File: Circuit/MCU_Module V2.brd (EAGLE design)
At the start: 160 x 100 mm, 44 parts, among them IC1 75176BD, Q1 8MHZ, T1 BC848, T2 BC848

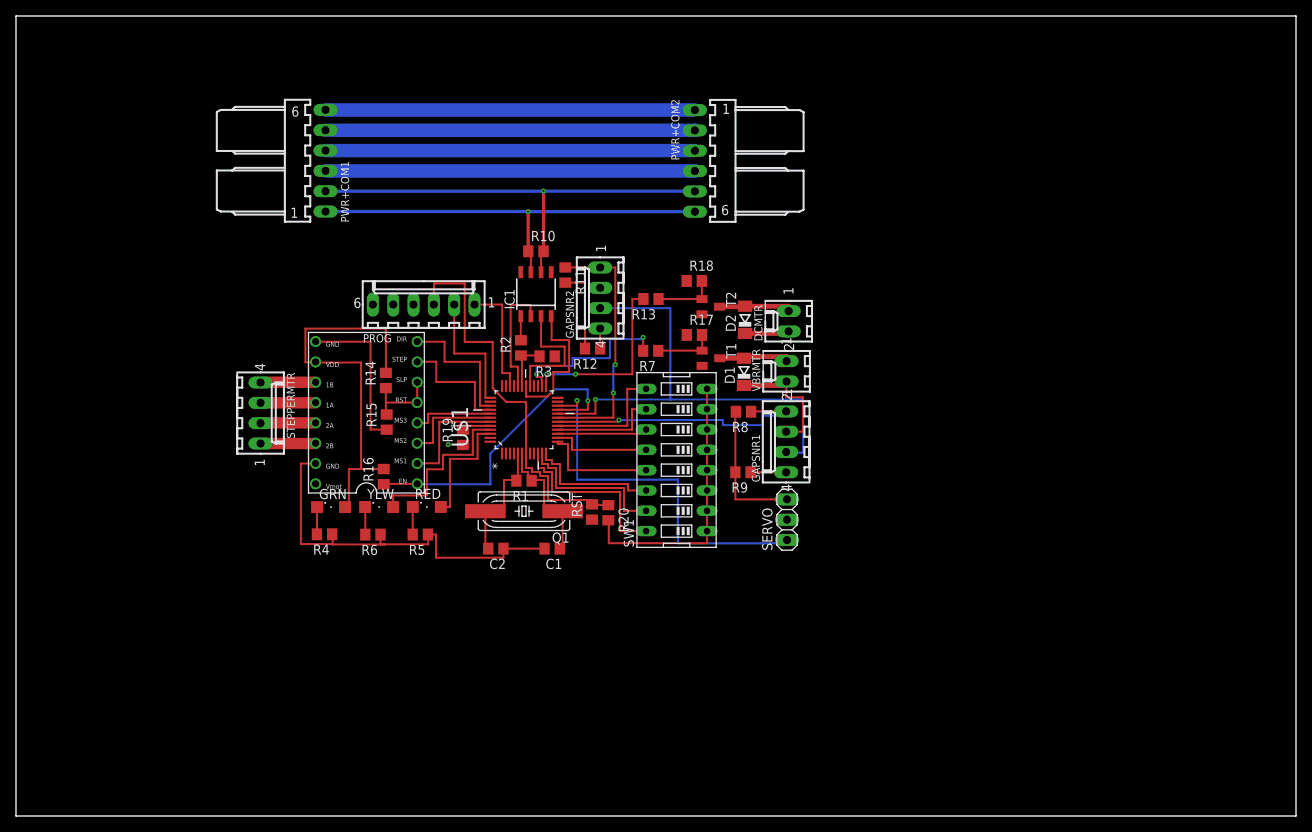
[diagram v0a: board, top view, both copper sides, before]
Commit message: redid layout and updated document
updated the document and redid the layout to improve layout and added
more initilizaton to the document
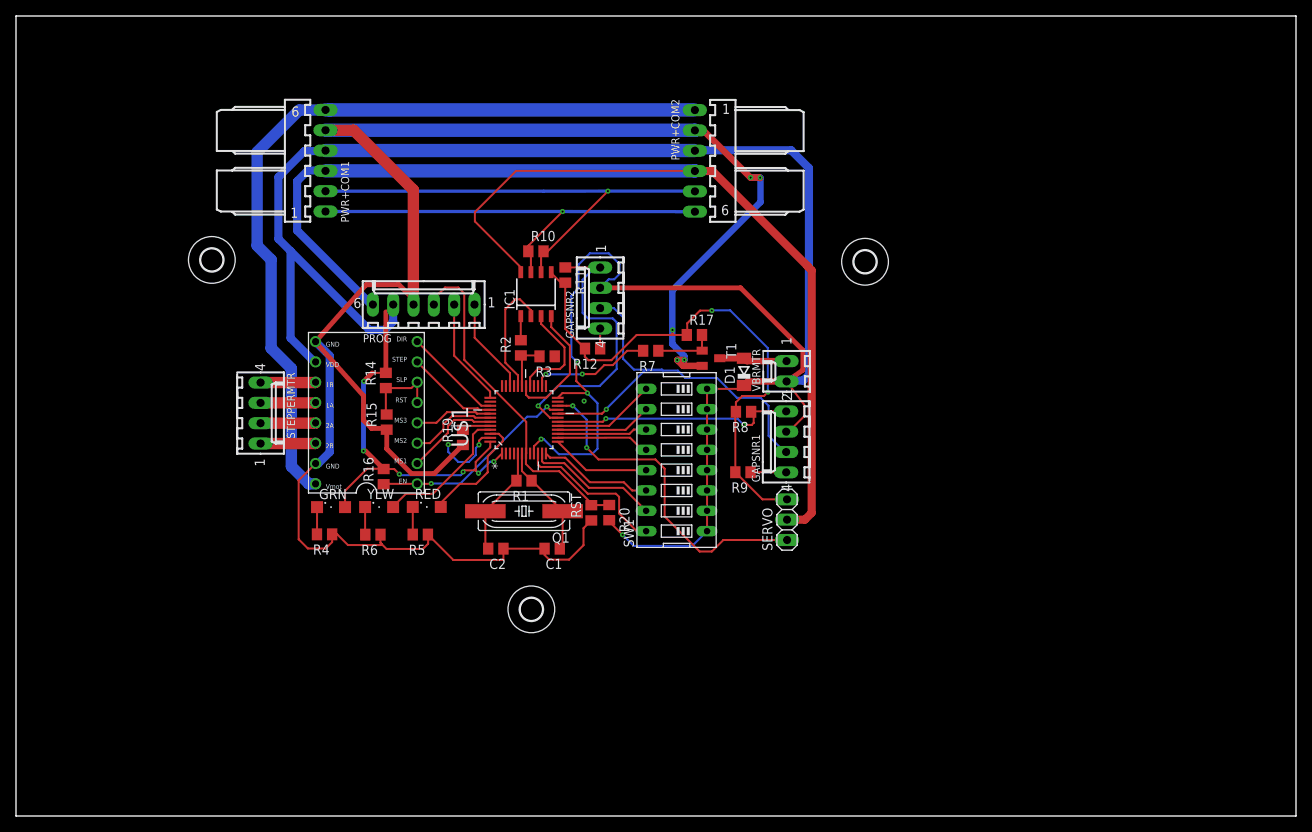
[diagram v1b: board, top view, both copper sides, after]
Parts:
- removed D2: LL4148, diode:SOD80C
- removed DCMTR: DCMOTOR, con-molex:6410-02
- removed R13: 120, rcl:R0805
- removed R18: 10k, rcl:R0805
- removed T2: BC848, transistor:SOT23
- added U$3, U$4, U$5: (no value), holes:2,8
- moved RST 0.13 mm to (71.9, 37.9)
- moved R20 0.11 mm to (74.2, 37.9)
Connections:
- removed net DCMTR: R13.2, U$1.25
- removed net MTR2-: D2.A, DCMTR.1, T2.3
- removed net N$4: R13.1, R18.2, T2.1
- net 5V: no longer D2.C, DCMTR.2
- net GND: no longer R18.1, T2.2
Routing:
- net 3V3: track 146.7 -> 330.6 mm, vias 0 -> 10
- net GND: track 145.0 -> 323.9 mm, vias 0 -> 9
- net 5V: track 51.9 -> 162.8 mm
- net 12V: track 46.2 -> 102.4 mm
- net DCMTR: track 23.1 -> 0.00 mm, vias 2 -> 0
- net EN: track 39.1 -> 25.9 mm, vias 1 -> 2
- net IRLED: track 61.5 -> 51.3 mm
- net MTR2-: track 9.29 -> 0.00 mm
- net NRST: track 51.2 -> 42.7 mm
- net N$4: track 7.73 -> 0.00 mm
- net VBRMTR: track 21.7 -> 15.5 mm
- net SGNL: track 47.6 -> 42.3 mm, vias 1 -> 2
- net DIR: track 17.2 -> 12.5 mm
- net VSENSE2: track 32.2 -> 36.7 mm, vias 2 -> 1
- net MCUSYS: track 21.8 -> 17.6 mm
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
